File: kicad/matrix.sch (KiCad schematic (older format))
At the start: 20 parts, among them J1 Conn_01x08, Q1 2N7002DW-7-F, Q2 2N7002DW-7-F, Q3 2N7002DW-7-F, Q4 2N7002DW-7-F, Q5 2N7002DW-7-F, Q6 2N7002DW-7-F, Q7 2N7002DW-7-F, Q8 2N7002DW-7-F, U1 TLC59025, U2 74HC595, U3 74HC595

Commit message: Add datasheets and long pad footprints
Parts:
- Q1, Q2, Q3, Q4, Q5, Q6, Q7, Q8: footprint digikey-footprints:SOT-363 -> Package_TO_SOT_SMD:SOT-363_SC-70-6_Handsoldering
- U2, U3: footprint Package_SO:SOIC-16_3.9x9.9mm_P1.27mm -> local:SOIC-16_3.9x9.9mm_P1.27mm_widepads
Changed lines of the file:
@@
 F 0 "U3" H 2250 4250 50  0000 R CNN
 F 1 "74HC595" V 2075 3700 50  0000 R CNN
-F 2 "Package_SO:SOIC-16_3.9x9.9mm_P1.27mm" H 2075 3700 50  0001 C CNN
+F 2 "local:SOIC-16_3.9x9.9mm_P1.27mm_widepads" H 2075 3700 50  0001 C CNN
 F 3 "http://www.ti.com/lit/ds/symlink/sn74hc595.pdf" H 2075 3700 50  0001 C CNN
 	1    2075 3700
@@
 F 0 "U2" H 2250 2700 50  0000 R CNN
 F 1 "74HC595" V 2075 2175 50  0000 R CNN
-F 2 "Package_SO:SOIC-16_3.9x9.9mm_P1.27mm" H 2075 2150 50  0001 C CNN
+F 2 "local:SOIC-16_3.9x9.9mm_P1.27mm_widepads" H 2075 2150 50  0001 C CNN
 F 3 "http://www.ti.com/lit/ds/symlink/sn74hc595.pdf" H 2075 2150 50  0001 C CNN
 	1    2075 2150
@@
 F 0 "Q1" V 3597 1778 60  0000 L CNN
 F 1 "2N7002DW-7-F" V 3500 975 60  0000 L CNN
-F 2 "digikey-footprints:SOT-363" H 3850 1650 60  0001 L CNN
+F 2 "Package_TO_SOT_SMD:SOT-363_SC-70-6_Handsoldering" H 3850 1650 60  0001 L CNN
 F 3 "https://www.diodes.com/assets/Datasheets/ds30120.pdf" H 3850 1750 60  0001 L CNN
 F 4 "2N7002DW-FDICT-ND" H 3850 1850 60  0001 L CNN "Digi-Key_PN"
@@
 F 0 "Q5" V 4697 1778 60  0000 L CNN
 F 1 "2N7002DW-7-F" V 4600 975 60  0000 L CNN
-F 2 "digikey-footprints:SOT-363" H 4950 1650 60  0001 L CNN
+F 2 "Package_TO_SOT_SMD:SOT-363_SC-70-6_Handsoldering" H 4950 1650 60  0001 L CNN
 F 3 "https://www.diodes.com/assets/Datasheets/ds30120.pdf" H 4950 1750 60  0001 L CNN
 F 4 "2N7002DW-FDICT-ND" H 4950 1850 60  0001 L CNN "Digi-Key_PN"
@@
 F 0 "Q2" V 3597 2653 60  0000 L CNN
 F 1 "2N7002DW-7-F" V 3500 1850 60  0000 L CNN
-F 2 "digikey-footprints:SOT-363" H 3850 2525 60  0001 L CNN
+F 2 "Package_TO_SOT_SMD:SOT-363_SC-70-6_Handsoldering" H 3850 2525 60  0001 L CNN
 F 3 "https://www.diodes.com/assets/Datasheets/ds30120.pdf" H 3850 2625 60  0001 L CNN
 F 4 "2N7002DW-FDICT-ND" H 3850 2725 60  0001 L CNN "Digi-Key_PN"
@@
 F 0 "Q6" V 4697 2653 60  0000 L CNN
 F 1 "2N7002DW-7-F" V 4600 1850 60  0000 L CNN
-F 2 "digikey-footprints:SOT-363" H 4950 2525 60  0001 L CNN
+F 2 "Package_TO_SOT_SMD:SOT-363_SC-70-6_Handsoldering" H 4950 2525 60  0001 L CNN
 F 3 "https://www.diodes.com/assets/Datasheets/ds30120.pdf" H 4950 2625 60  0001 L CNN
 F 4 "2N7002DW-FDICT-ND" H 4950 2725 60  0001 L CNN "Digi-Key_PN"
@@
 F 0 "Q3" V 3597 3703 60  0000 L CNN
 F 1 "2N7002DW-7-F" V 3500 2900 60  0000 L CNN
-F 2 "digikey-footprints:SOT-363" H 3850 3575 60  0001 L CNN
+F 2 "Package_TO_SOT_SMD:SOT-363_SC-70-6_Handsoldering" H 3850 3575 60  0001 L CNN
 F 3 "https://www.diodes.com/assets/Datasheets/ds30120.pdf" H 3850 3675 60  0001 L CNN
 F 4 "2N7002DW-FDICT-ND" H 3850 3775 60  0001 L CNN "Digi-Key_PN"
@@
 F 0 "Q7" V 4697 3703 60  0000 L CNN
 F 1 "2N7002DW-7-F" V 4600 2900 60  0000 L CNN
-F 2 "digikey-footprints:SOT-363" H 4950 3575 60  0001 L CNN
+F 2 "Package_TO_SOT_SMD:SOT-363_SC-70-6_Handsoldering" H 4950 3575 60  0001 L CNN
 F 3 "https://www.diodes.com/assets/Datasheets/ds30120.pdf" H 4950 3675 60  0001 L CNN
 F 4 "2N7002DW-FDICT-ND" H 4950 3775 60  0001 L CNN "Digi-Key_PN"
@@
 F 0 "Q4" V 3597 4578 60  0000 L CNN
 F 1 "2N7002DW-7-F" V 3500 3775 60  0000 L CNN
-F 2 "digikey-footprints:SOT-363" H 3850 4450 60  0001 L CNN
+F 2 "Package_TO_SOT_SMD:SOT-363_SC-70-6_Handsoldering" H 3850 4450 60  0001 L CNN
 F 3 "https://www.diodes.com/assets/Datasheets/ds30120.pdf" H 3850 4550 60  0001 L CNN
 F 4 "2N7002DW-FDICT-ND" H 3850 4650 60  0001 L CNN "Digi-Key_PN"
@@
 F 0 "Q8" V 4697 4578 60  0000 L CNN
 F 1 "2N7002DW-7-F" V 4600 3775 60  0000 L CNN
-F 2 "digikey-footprints:SOT-363" H 4950 4450 60  0001 L CNN
+F 2 "Package_TO_SOT_SMD:SOT-363_SC-70-6_Handsoldering" H 4950 4450 60  0001 L CNN
 F 3 "https://www.diodes.com/assets/Datasheets/ds30120.pdf" H 4950 4550 60  0001 L CNN
 F 4 "2N7002DW-FDICT-ND" H 4950 4650 60  0001 L CNN "Digi-Key_PN"

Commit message: Enlarge display footprint and SMD pad widths
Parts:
- D1, D2, D3, D4: footprint akn_misc:LED_8x8_3MM_32x32MM -> local:LED_8x8_3MM_38x38MM
- U1: footprint Package_SO:SSOP-24_3.9x8.7mm_P0.635mm -> local:SSOP-24_3.9x8.7mm_P0.635mm_widepads
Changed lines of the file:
@@
 F 0 "D1" H 6700 4712 60  0000 C CNN
 F 1 "DISP_LED_MAT_8x8_COM_ANODE" H 6700 4606 60  0000 C CNN
-F 2 "akn_misc:LED_8x8_3MM_32x32MM" H 6125 3575 60  0001 C CNN
+F 2 "local:LED_8x8_3MM_38x38MM" H 6125 3575 60  0001 C CNN
 F 3 "" H 6125 3575 60  0000 C CNN
 	1    6025 3625
@@
 F 0 "D3" H 9475 4712 60  0000 C CNN
 F 1 "DISP_LED_MAT_8x8_COM_ANODE" H 9475 4606 60  0000 C CNN
-F 2 "akn_misc:LED_8x8_3MM_32x32MM" H 8900 3575 60  0001 C CNN
+F 2 "local:LED_8x8_3MM_38x38MM" H 8900 3575 60  0001 C CNN
 F 3 "" H 8900 3575 60  0000 C CNN
 	1    8800 3625
@@
 F 0 "D2" H 6700 7262 60  0000 C CNN
 F 1 "DISP_LED_MAT_8x8_COM_ANODE" H 6700 7156 60  0000 C CNN
-F 2 "akn_misc:LED_8x8_3MM_32x32MM" H 6125 6125 60  0001 C CNN
+F 2 "local:LED_8x8_3MM_38x38MM" H 6125 6125 60  0001 C CNN
 F 3 "" H 6125 6125 60  0000 C CNN
 	1    6025 6175
@@
 F 0 "D4" H 9475 7262 60  0000 C CNN
 F 1 "DISP_LED_MAT_8x8_COM_ANODE" H 9475 7156 60  0000 C CNN
-F 2 "akn_misc:LED_8x8_3MM_32x32MM" H 8900 6125 60  0001 C CNN
+F 2 "local:LED_8x8_3MM_38x38MM" H 8900 6125 60  0001 C CNN
 F 3 "" H 8900 6125 60  0000 C CNN
 	1    8800 6175
@@
 F 0 "U1" V 4150 4900 50  0000 R CNN
 F 1 "TLC59025" V 3650 5975 50  0000 R CNN
-F 2 "Package_SO:SSOP-24_3.9x8.7mm_P0.635mm" H 3650 5775 50  0001 C CNN
+F 2 "local:SSOP-24_3.9x8.7mm_P0.635mm_widepads" H 3650 5775 50  0001 C CNN
 F 3 "http://www.ti.com/lit/ds/symlink/tlc59025.pdf" H 3650 5775 50  0001 C CNN
 	1    3650 5775

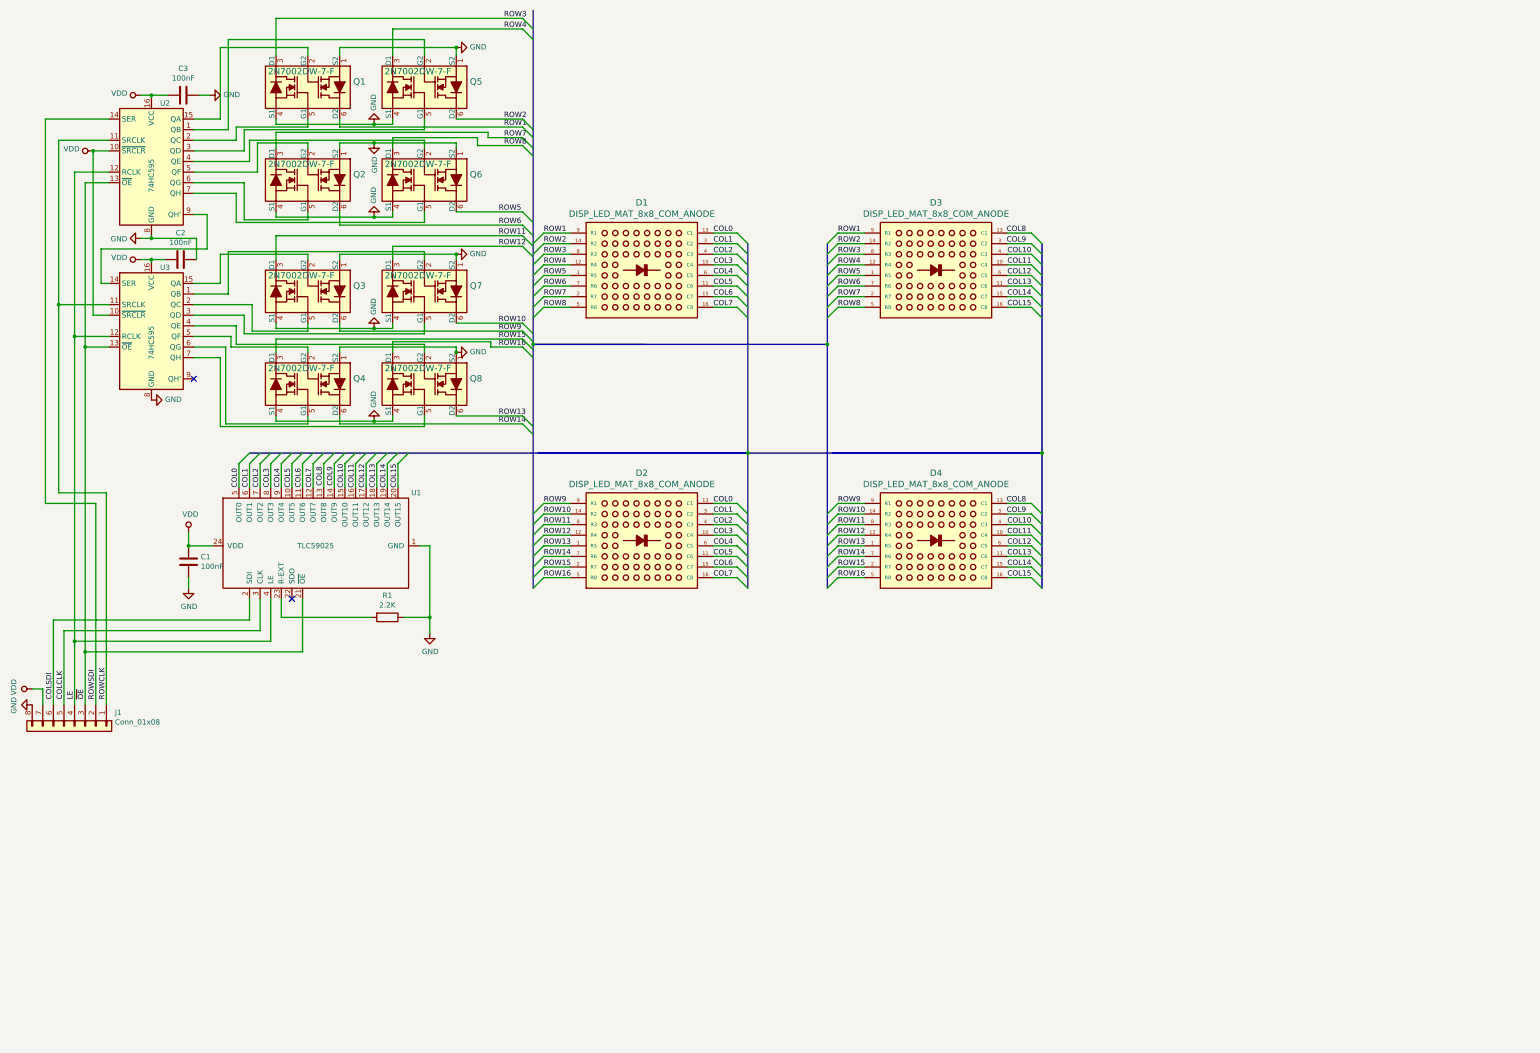
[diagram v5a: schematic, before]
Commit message: Switch to P-channel FETs in SOIC-8 package
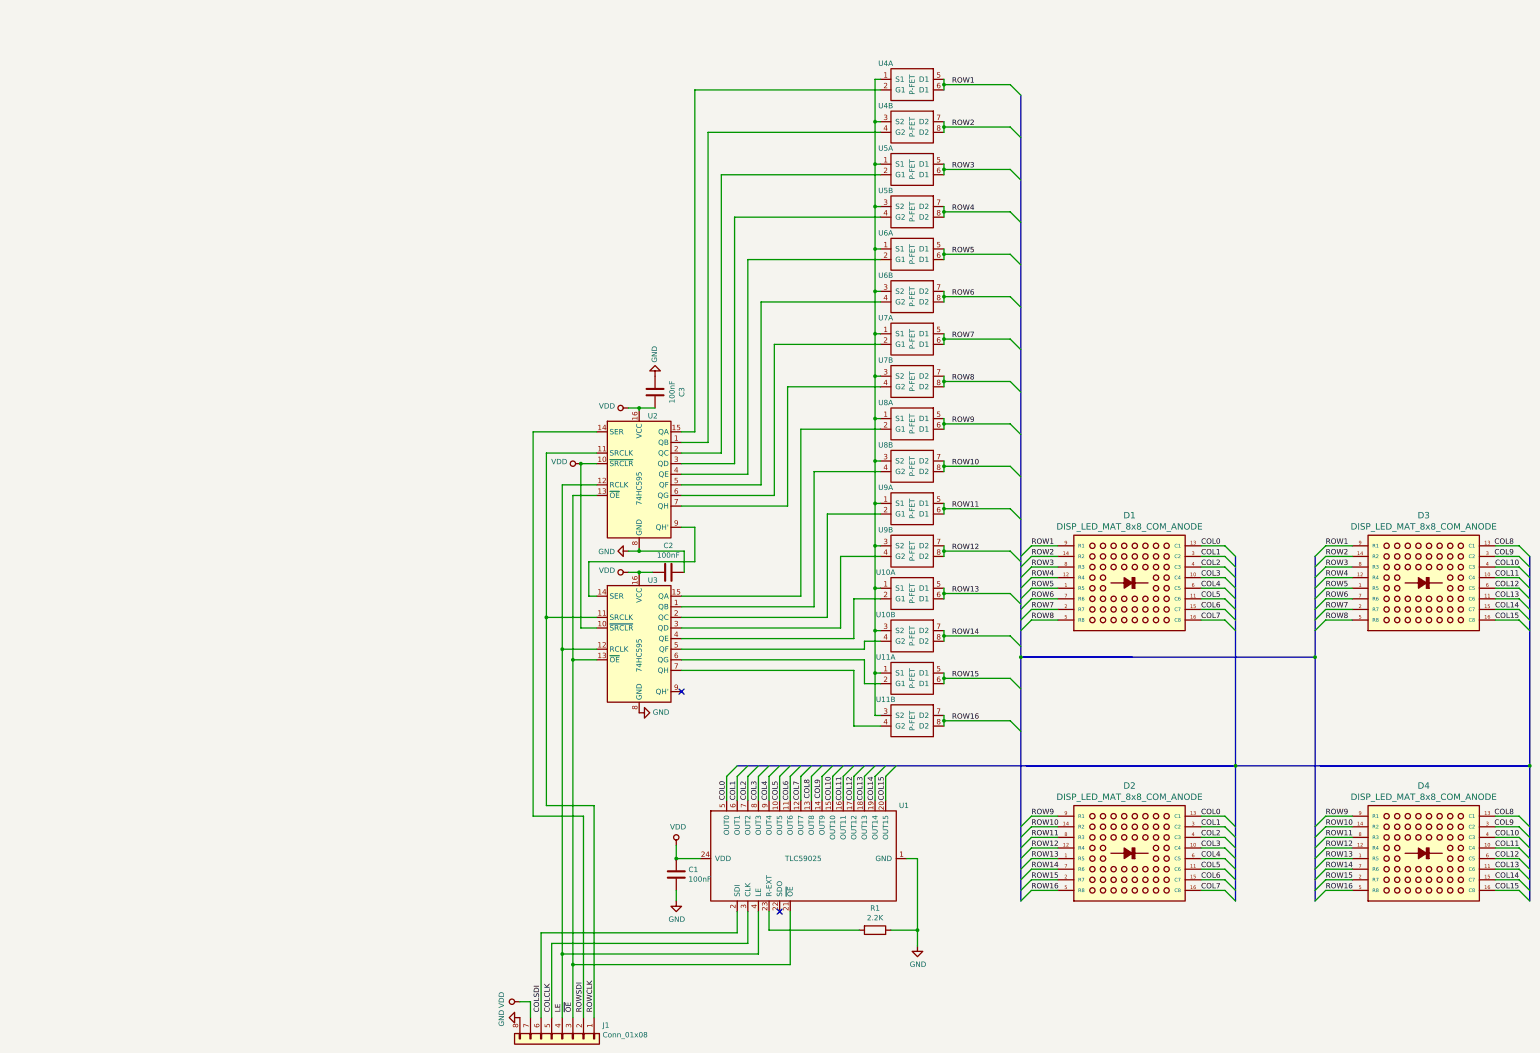
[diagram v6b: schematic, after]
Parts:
- removed Q1, Q2, Q3, Q4, Q5, Q6, Q7, Q8: 2N7002DW-7-F, Package_TO_SOT_SMD:SOT-363_SC-70-6_Handsoldering, symbol dk_Transistors-FETs-MOSFETs-Arrays:2N7002DW-7-F
- added U10, U11, U4, U5, U6, U7, U8, U9: P-FET, local:SOIC-8_3.9x4.9mm_P1.27mm_widepads, symbol local:P-FET
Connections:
- net GND: now also C3.2; no longer C3.1
- net ROW1: now also U4.5 (D1), U4.6 (D1)
- net ROW10: now also U8.7 (D2), U8.8 (D2)
- net ROW11: now also U9.5 (D1), U9.6 (D1)
- net ROW12: now also U9.7 (D2), U9.8 (D2)
- net ROW13: now also U10.5 (D1), U10.6 (D1)
- net ROW14: now also U10.7 (D2), U10.8 (D2)
- net ROW15: now also U11.5 (D1), U11.6 (D1)
- net ROW16: now also U11.7 (D2), U11.8 (D2)
- net ROW2: now also U4.7 (D2), U4.8 (D2)
- net ROW3: now also U5.5 (D1), U5.6 (D1)
- net ROW4: now also U5.7 (D2), U5.8 (D2)
- net ROW5: now also U6.5 (D1), U6.6 (D1)
- net ROW6: now also U6.7 (D2), U6.8 (D2)
- net ROW7: now also U7.5 (D1), U7.6 (D1)
- net ROW8: now also U7.7 (D2), U7.8 (D2)
- net ROW9: now also U8.5 (D1), U8.6 (D1)
- net VDD: now also C3.1; no longer C3.2
- net at U3.1 (QB): now also U8.4 (G2)
- net at U3.15 (QA): now also U8.2 (G1)
- net at U3.2 (QC): now also U9.2 (G1)
- net at U3.3 (QD): now also U9.4 (G2)
- net at U3.4 (QE): now also U10.2 (G1)
- net at U3.5 (QF): now also U10.4 (G2)
- net at U3.6 (QG): now also U11.2 (G1)
- net at U3.7 (QH): now also U11.4 (G2)
- net at U2.1 (QB): now also U4.4 (G2)
- net at U2.15 (QA): now also U4.2 (G1)
- net at U2.2 (QC): now also U5.2 (G1)
- net at U2.3 (QD): now also U5.4 (G2)
- net at U2.4 (QE): now also U6.2 (G1)
- net at U2.5 (QF): now also U6.4 (G2)
- net at U2.6 (QG): now also U7.2 (G1)
- net at U2.7 (QH): now also U7.4 (G2)
- new net: U10.1 (S1), U10.3 (S2), U11.1 (S1), U11.3 (S2), U4.1 (S1), U4.3 (S2), U5.1 (S1), U5.3 (S2), U6.1 (S1), U6.3 (S2), U7.1 (S1), U7.3 (S2), U8.1 (S1), U8.3 (S2), U9.1 (S1), U9.3 (S2)
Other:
- moved on the sheet: C1, C2, C3, D1, D2, D3, D4, J1, R1, U1, U2, U3

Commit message: Add power net
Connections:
- net VDD: now also U10.1 (S1), U10.3 (S2), U11.1 (S1), U11.3 (S2), U4.1 (S1), U4.3 (S2), U5.1 (S1), U5.3 (S2), U6.1 (S1), U6.3 (S2), U7.1 (S1), U7.3 (S2), U8.1 (S1), U8.3 (S2), U9.1 (S1), U9.3 (S2)
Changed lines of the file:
@@
 Wire Bus Line
 	10275 1525 10275 6825
+$Comp
+L power:VDD #PWR?
+U 1 1 5F638642
+P 8900 1375
+F 0 "#PWR?" H 8900 1225 50  0001 C CNN
+F 1 "VDD" V 8918 1502 50  0000 L CNN
+F 2 "" H 8900 1375 50  0001 C CNN
+F 3 "" H 8900 1375 50  0001 C CNN
+	1    8900 1375
+	0    -1   -1   0
+$EndComp
+Connection ~ 8900 1375
 $EndSCHEMATC

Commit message: Finished most of the layout
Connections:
- net COLCLK: now also J1.2 (Pin_2); no longer J1.5 (Pin_5)
- net COLSDI: now also J1.3 (Pin_3); no longer J1.6 (Pin_6)
- net LE: now also J1.1 (Pin_1); no longer J1.4 (Pin_4)
- net ROWCLK: now also J1.6 (Pin_6); no longer J1.1 (Pin_1)
- net ROWSDI: now also J1.5 (Pin_5); no longer J1.2 (Pin_2)
- net ~OE: now also J1.4 (Pin_4); no longer J1.3 (Pin_3)
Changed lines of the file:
@@
 $EndComp
 Wire Wire Line
-	6275 5300 6050 5300
-Wire Wire Line
-	6050 5300 6050 6850
-Wire Wire Line
-	6050 6850 6275 6850
-Wire Wire Line
-	6275 4900 5800 4900
-Wire Wire Line
-	5800 4900 5800 6450
-Wire Wire Line
-	5800 6450 6275 6450
+	6275 5300 5950 5300
+Wire Wire Line
+	5950 5300 5950 6850
+Wire Wire Line
+	5950 6850 6275 6850
+Wire Wire Line
+	6275 4900 5750 4900
+Wire Wire Line
+	5750 4900 5750 6450
+Wire Wire Line
+	5750 6450 6275 6450
 $Comp
 L power:VDD #PWR03
@@
 Wire Wire Line
 	6675 4475 6675 4500
-Text Label 6050 10175 1    50   ~ 0
+Text Label 5950 10175 1    50   ~ 0
 ~OE
 NoConn ~ 7075 7150
@@
 L power:GND #PWR017
 U 1 1 5EE44BE5
-P 5550 10225
-F 0 "#PWR017" H 5550 9975 50  0001 C CNN
-F 1 "GND" H 5555 10052 50  0000 C CNN
-F 2 "" H 5550 10225 50  0001 C CNN
-F 3 "" H 5550 10225 50  0001 C CNN
-	1    5550 10225
+P 5275 9925
+F 0 "#PWR017" H 5275 9675 50  0001 C CNN
+F 1 "GND" H 5280 9752 50  0000 C CNN
+F 2 "" H 5275 9925 50  0001 C CNN
+F 3 "" H 5275 9925 50  0001 C CNN
+	1    5275 9925
 	0    1    1    0
 $EndComp
@@
 L power:VDD #PWR016
 U 1 1 5EE456DF
-P 5550 10075
-F 0 "#PWR016" H 5550 9925 50  0001 C CNN
-F 1 "VDD" H 5567 10248 50  0000 C CNN
-F 2 "" H 5550 10075 50  0001 C CNN
-F 3 "" H 5550 10075 50  0001 C CNN
-	1    5550 10075
+P 5275 9500
+F 0 "#PWR016" H 5275 9350 50  0001 C CNN
+F 1 "VDD" H 5292 9673 50  0000 C CNN
+F 2 "" H 5275 9500 50  0001 C CNN
+F 3 "" H 5275 9500 50  0001 C CNN
+	1    5275 9500
 	0    -1   -1   0
 $EndComp
 Wire Wire Line
-	5550 10075 5650 10075
-Wire Wire Line
-	5650 10075 5650 10225
+	5275 9500 5375 9500
 Wire Wire Line
 	7600 9225 7600 9425
 Wire Wire Line
-	7600 9425 5750 9425
-Wire Wire Line
-	5750 9425 5750 10225
-Wire Wire Line
 	7700 9225 7700 9525
 Wire Wire Line
-	7700 9525 5850 9525
-Wire Wire Line
-	5850 9525 5850 10225
-Wire Wire Line
 	7800 9225 7800 9625
 Wire Wire Line
-	7800 9625 5950 9625
-Wire Wire Line
-	5950 9625 5950 10225
-Wire Wire Line
-	8100 9725 6050 9725
-Wire Wire Line
-	6050 9725 6050 10225
+	8100 9725 5950 9725
 Wire Wire Line
 	8100 9225 8100 9725
 Wire Wire Line
-	6050 6850 6050 9725
-Connection ~ 6050 6850
-Connection ~ 6050 9725
-Wire Wire Line
-	6275 4700 5675 4700
-Wire Wire Line
-	5675 4700 5675 8325
-Wire Wire Line
-	5675 8325 6150 8325
-Wire Wire Line
-	6150 8325 6150 10225
+	5950 6850 5950 9725
+Connection ~ 5950 6850
 $Comp
 L power:VDD #PWR018
@@
 	6125 6550 6275 6550
 Connection ~ 6125 5000
+Text Label 6050 10175 1    50   ~ 0
+COLSDI
+Text Label 6150 10175 1    50   ~ 0
+COLCLK
+Text Label 6250 10175 1    50   ~ 0
+LE
+Wire Wire Line
+	6050 6750 6275 6750
+Wire Wire Line
+	6050 6750 6050 5200
+Wire Wire Line
+	6050 5200 6275 5200
+Text Label 5850 10175 1    50   ~ 0
+ROWSDI
+Connection ~ 5750 6450
 Text Label 5750 10175 1    50   ~ 0
-COLSDI
-Text Label 5850 10175 1    50   ~ 0
-COLCLK
-Text Label 5950 10175 1    50   ~ 0
-LE
-Wire Wire Line
-	5950 9625 5950 6750
-Wire Wire Line
-	5950 6750 6275 6750
-Connection ~ 5950 9625
-Wire Wire Line
-	5950 6750 5950 5200
-Wire Wire Line
-	5950 5200 6275 5200
-Connection ~ 5950 6750
-Text Label 6150 10175 1    50   ~ 0
-ROWSDI
-Wire Wire Line
-	5800 6450 5800 8225
-Wire Wire Line
-	5800 8225 6250 8225
-Wire Wire Line
-	6250 8225 6250 10225
-Connection ~ 5800 6450
-Text Label 6250 10175 1    50   ~ 0
 ROWCLK
 $Comp
@@
 Wire Wire Line
 	7200 1475 8950 1475
-Wire Bus Line
-	10275 6825 10275 9125
-Wire Bus Line
-	13050 6825 13050 9125
-Wire Bus Line
-	13050 5875 13050 6825
-Wire Bus Line
-	15075 7850 15075 9125
-Wire Bus Line
-	15075 5875 15075 7850
-Wire Bus Line
-	12300 7850 12300 9125
-Wire Bus Line
-	12300 5875 12300 7850
-Wire Bus Line
-	7600 7850 12300 7850
-Wire Bus Line
-	10275 1525 10275 6825
-$Comp
-L power:VDD #PWR?
+$Comp
+L power:VDD #PWR0101
 U 1 1 5F638642
 P 8900 1375
-F 0 "#PWR?" H 8900 1225 50  0001 C CNN
+F 0 "#PWR0101" H 8900 1225 50  0001 C CNN
 F 1 "VDD" V 8918 1502 50  0000 L CNN
 F 2 "" H 8900 1375 50  0001 C CNN
@@
 $EndComp
 Connection ~ 8900 1375
+Wire Wire Line
+	5750 6450 5750 10225
+Wire Wire Line
+	5850 4700 5850 10225
+Wire Wire Line
+	5850 4700 6275 4700
+Wire Wire Line
+	5950 9725 5950 10225
+Connection ~ 5950 9725
+Wire Wire Line
+	6050 9425 6050 10225
+Wire Wire Line
+	6050 9425 7600 9425
+Wire Wire Line
+	6150 9525 6150 10225
+Wire Wire Line
+	6150 9525 7700 9525
+Wire Wire Line
+	7800 9625 6250 9625
+Wire Wire Line
+	6250 9625 6250 10225
+Wire Wire Line
+	6050 6750 6050 9325
+Wire Wire Line
+	6050 9325 6250 9325
+Wire Wire Line
+	6250 9325 6250 9625
+Connection ~ 6050 6750
+Connection ~ 6250 9625
+Wire Wire Line
+	5550 9925 5550 10225
+$Comp
+L power:PWR_FLAG #FLG0101
+U 1 1 5F939576
+P 5375 9500
+F 0 "#FLG0101" H 5375 9575 50  0001 C CNN
+F 1 "PWR_FLAG" H 5375 9673 50  0000 C CNN
+F 2 "" H 5375 9500 50  0001 C CNN
+F 3 "~" H 5375 9500 50  0001 C CNN
+	1    5375 9500
+	1    0    0    -1
+$EndComp
+Wire Wire Line
+	5650 10225 5650 9500
+Wire Wire Line
+	5650 9500 5375 9500
+Connection ~ 5375 9500
+Wire Wire Line
+	5550 9925 5375 9925
+Wire Bus Line
+	10275 6825 10275 9125
+Wire Bus Line
+	13050 6825 13050 9125
+Wire Bus Line
+	13050 5875 13050 6825
+Wire Bus Line
+	15075 7850 15075 9125
+Wire Bus Line
+	15075 5875 15075 7850
+Wire Bus Line
+	12300 7850 12300 9125
+Wire Bus Line
+	12300 5875 12300 7850
+Wire Bus Line
+	7600 7850 12300 7850
+Wire Bus Line
+	10275 1525 10275 6825
+$Comp
+L power:PWR_FLAG #FLG0102
+U 1 1 5F996FD8
+P 5375 9925
+F 0 "#FLG0102" H 5375 10000 50  0001 C CNN
+F 1 "PWR_FLAG" H 5375 10098 50  0000 C CNN
+F 2 "" H 5375 9925 50  0001 C CNN
+F 3 "~" H 5375 9925 50  0001 C CNN
+	1    5375 9925
+	1    0    0    -1
+$EndComp
+Connection ~ 5375 9925
+Wire Wire Line
+	5375 9925 5275 9925
 $EndSCHEMATC
